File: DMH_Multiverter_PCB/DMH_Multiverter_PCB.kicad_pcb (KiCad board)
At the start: 2 copper layers, 48 x 175 mm, 0 parts

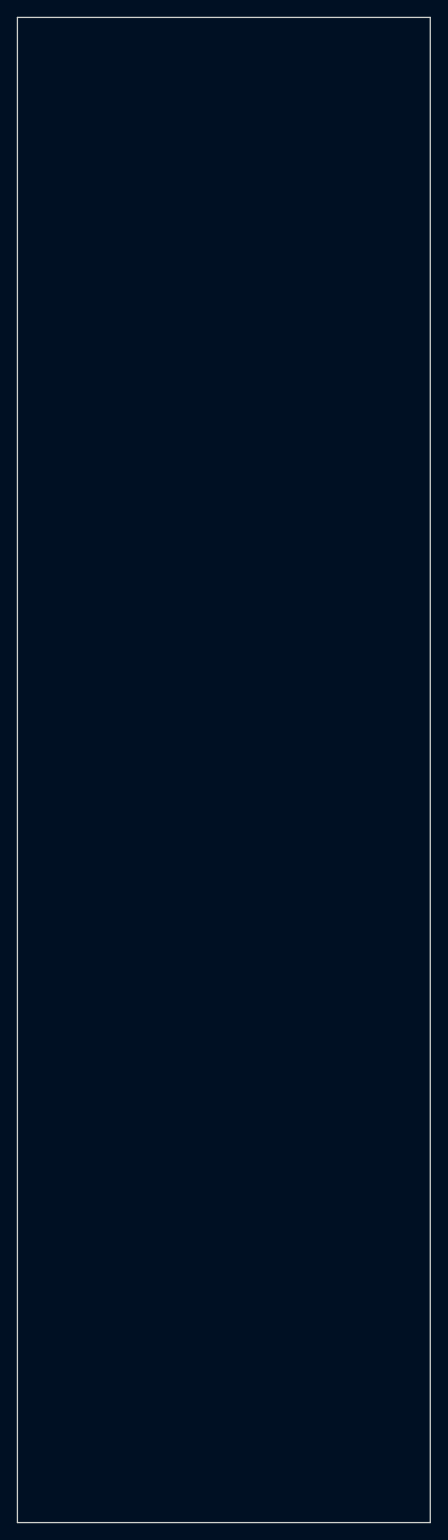
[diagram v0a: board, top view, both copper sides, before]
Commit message: Placed components in PCB
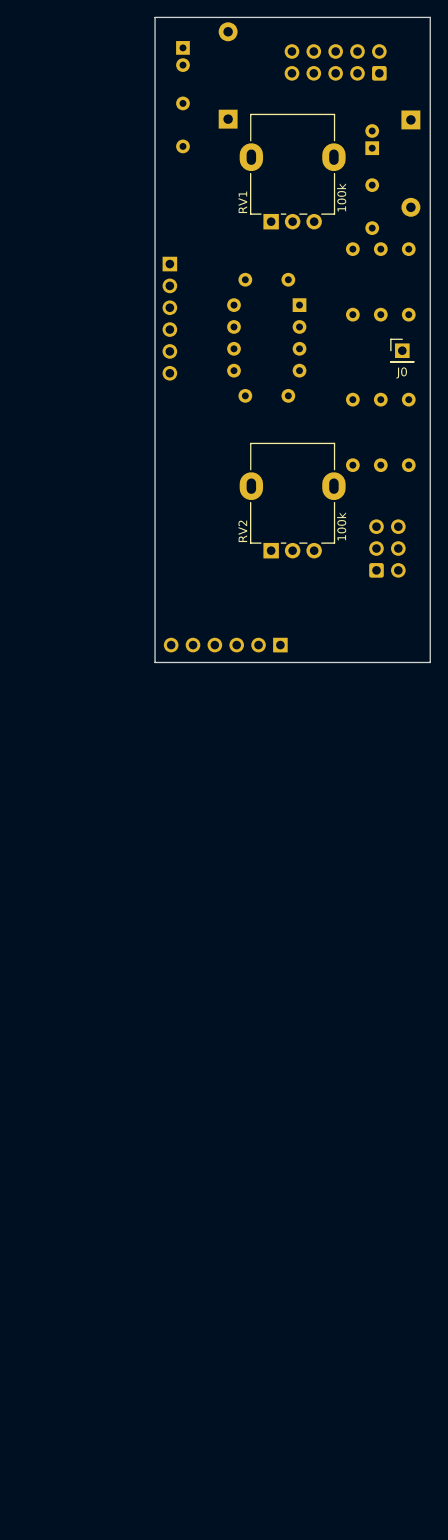
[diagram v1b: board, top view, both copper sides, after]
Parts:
- added C1: 47uF, Capacitor_THT:CP_Radial_D5.0mm_P2.00mm, B.Cu at (70.2, 46.0)
- added C2: 47uF, Capacitor_THT:CP_Radial_D5.0mm_P2.00mm, B.Cu at (92.2, 57.7)
- added C3: 100nF, Capacitor_THT:C_Disc_D4.3mm_W1.9mm_P5.00mm, B.Cu at (70.2, 57.5)
- added C4: 100nF, Capacitor_THT:C_Disc_D4.3mm_W1.9mm_P5.00mm, B.Cu at (92.2, 62.0)
- added C5: 100nF, Capacitor_THT:C_Disc_D4.3mm_W1.9mm_P5.00mm, B.Cu at (77.5, 73.0)
- added C6: 100nF, Capacitor_THT:C_Disc_D4.3mm_W1.9mm_P5.00mm, B.Cu at (82.5, 86.5)
- added D1: SB140+, Diode_THT:D_DO-41_SOD81_P10.16mm_Horizontal, B.Cu at (75.5, 54.3)
- added D2: SB140-, Diode_THT:D_DO-41_SOD81_P10.16mm_Horizontal, B.Cu at (96.8, 54.4)
- added J0: Conn_01x01, Connector_PinHeader_2.54mm:PinHeader_1x01_P2.54mm_Vertical, F.Cu at (95.8, 81.2)
- added J100: IDC_02x05, SynthStuff:IDC-Header_2x05_P2.54mm_Vertical_Eurorack, B.Cu at (93.1, 49.0)
- added J200: BackBone_Connector_6pin, SynthStuff:IDC-Header_2x03_P2.54mm_Vertical_BackBone, B.Cu at (92.7, 106.8)
- added J50: Conn_01x06, Connector_PinSocket_2.54mm:PinSocket_1x06_P2.54mm_Vertical, B.Cu at (68.7, 71.2)
- added J60: Conn_01x06, Connector_PinSocket_2.54mm:PinSocket_1x06_P2.54mm_Vertical, B.Cu at (81.6, 115.5)
- added R1: 100k, Resistor_THT:R_Axial_DIN0207_L6.3mm_D2.5mm_P7.62mm_Horizontal, B.Cu at (90.0, 69.4)
- added R2: 100k, Resistor_THT:R_Axial_DIN0207_L6.3mm_D2.5mm_P7.62mm_Horizontal, B.Cu at (93.2, 77.1)
- added R3: 1k, Resistor_THT:R_Axial_DIN0207_L6.3mm_D2.5mm_P7.62mm_Horizontal, B.Cu at (96.5, 69.4)
- added R4: 100k, Resistor_THT:R_Axial_DIN0207_L6.3mm_D2.5mm_P7.62mm_Horizontal, B.Cu at (90.0, 94.6)
- added R5: 100k, Resistor_THT:R_Axial_DIN0207_L6.3mm_D2.5mm_P7.62mm_Horizontal, B.Cu at (93.2, 94.6)
- added R6: 1k, Resistor_THT:R_Axial_DIN0207_L6.3mm_D2.5mm_P7.62mm_Horizontal, B.Cu at (96.5, 86.9)
- added RV1: 100k, SynthStuff:Potentiometer_Alpha_RD901F-40-00D_Single_Vertical, F.Cu at (80.5, 66.2)
- added RV2: 100k, SynthStuff:Potentiometer_Alpha_RD901F-40-00D_Single_Vertical, F.Cu at (80.5, 104.5)
- added U1: TL072, Package_DIP:DIP-8_W7.62mm_Socket, B.Cu at (83.8, 76.0)
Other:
- board size 48 x 175 mm -> 32 x 75 mm

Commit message: Finished PCB Conn schematic
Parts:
- moved C6 5.00 mm to (77.5, 86.5), turned to 0 degrees
- moved J50 0.25 mm to (69.0, 71.2)
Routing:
- net -12V: track 0.00 -> 46.5 mm
- net /Core Circuit/Att B Input: track 0.00 -> 40.4 mm
- net +12V: track 0.00 -> 40.1 mm
- net /Core Circuit/Att B Output: track 0.00 -> 35.7 mm
- net /Core Circuit/Att A Output: track 0.00 -> 30.0 mm
- net Net-(J200-Pin_4): track 0.00 -> 26.0 mm
- net Net-(U1B--): track 0.00 -> 25.2 mm
- net /Core Circuit/Att A Input: track 0.00 -> 24.4 mm
- net Net-(R5-Pad2): track 0.00 -> 23.8 mm
- net Net-(U1B-+): track 0.00 -> 23.8 mm
- net Net-(J200-Pin_3): track 0.00 -> 22.0 mm
- net Net-(J200-Pin_2): track 0.00 -> 18.4 mm
- net Net-(U1A-+): track 0.00 -> 16.5 mm
- net Net-(R2-Pad2): track 0.00 -> 15.4 mm
- net Net-(J200-Pin_1): track 0.00 -> 14.8 mm
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- added copper zone on B.Cu, net GND
- added copper zone on F.Cu, net GND

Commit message: Finished conn PCB
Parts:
- moved C1 9.09 mm to (75.0, 53.8)
- moved J60 7.75 mm to (89.3, 115.5)
- moved D1 5.80 mm to (69.8, 55.1)
- moved C3 2.30 mm to (69.8, 59.8), turned to -90 degrees
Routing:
- net +12V: track 40.1 -> 30.4 mm
- net Net-(D1-A): track 10.9 -> 16.3 mm
- net Net-(J200-Pin_4): track 26.0 -> 21.3 mm
- net Net-(J200-Pin_2): track 18.4 -> 13.7 mm
- net Net-(J200-Pin_1): track 14.8 -> 10.1 mm
- net Net-(J200-Pin_3): track 22.0 -> 17.3 mm

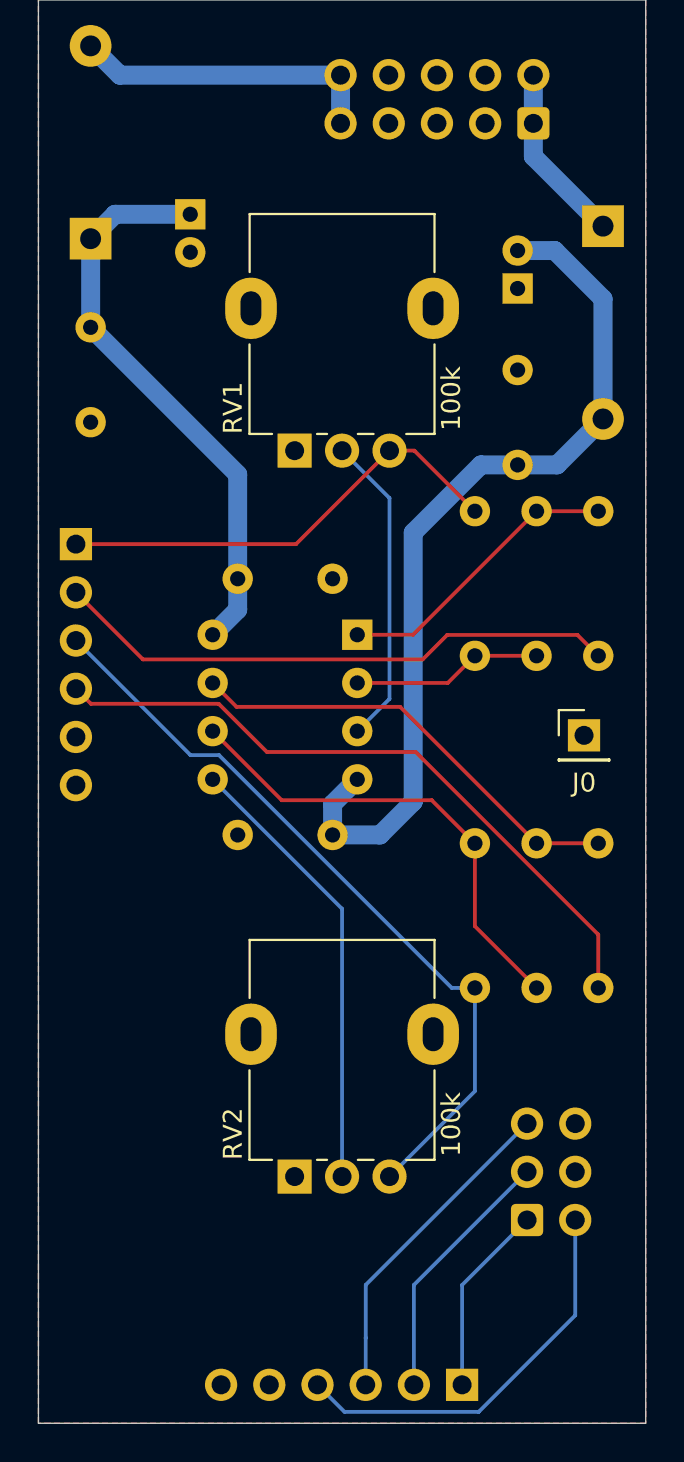
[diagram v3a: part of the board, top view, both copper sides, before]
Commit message: Adapted design to center detent pot P110KH-1F15
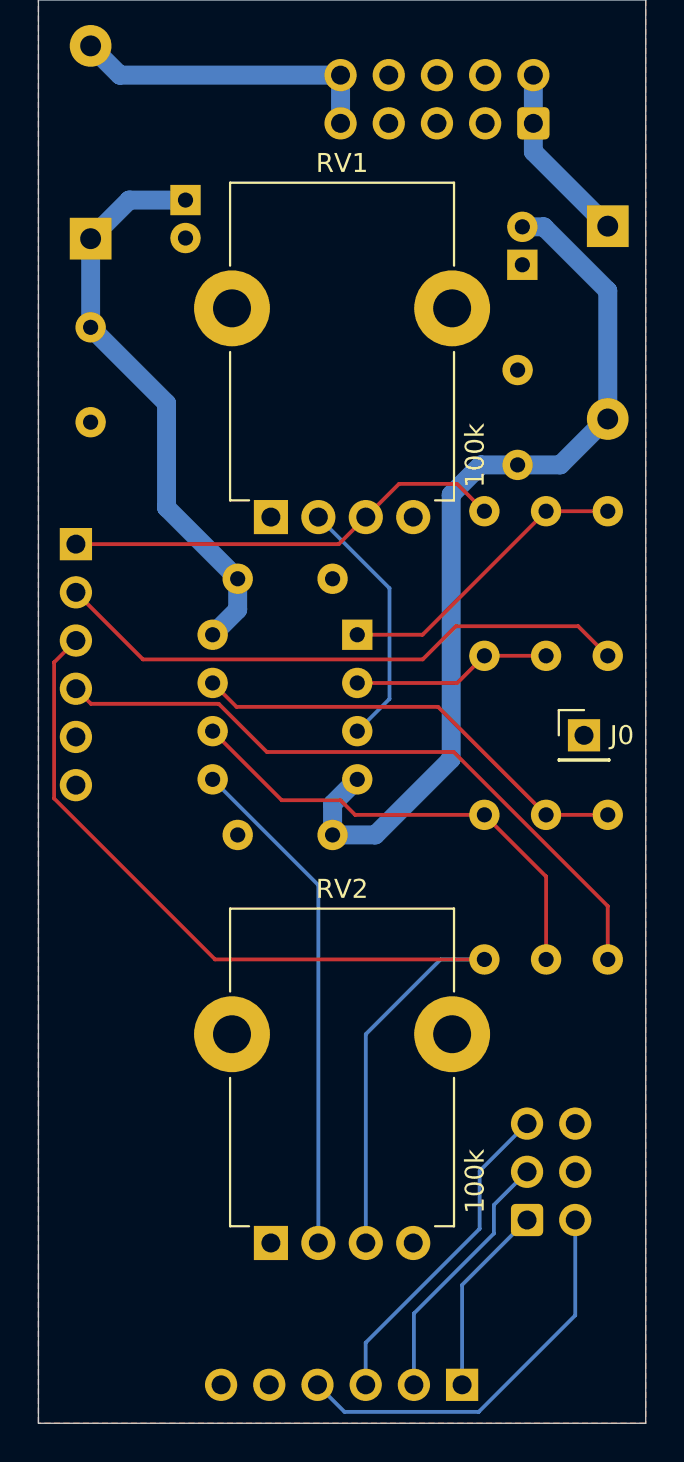
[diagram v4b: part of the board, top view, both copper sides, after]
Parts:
- RV1, RV2: footprint SynthStuff:Potentiometer_Alpha_RD901F-40-00D_Single_Vertical -> SynthStuff:Potentiometer_TT_P110KH1
- moved RV1 3.50 mm to (80.5, 69.8), turned to 0 degrees
- moved RV2 3.50 mm to (80.5, 108.0), turned to 0 degrees
- moved R4 1.58 mm to (90.5, 93.1)
- moved R5 1.58 mm to (93.8, 93.1)
- moved R6 1.58 mm to (97.0, 85.4)
- moved C2 1.27 mm to (92.5, 56.5)
- moved C1 0.79 mm to (74.8, 53.0)
- moved R1 0.50 mm to (90.5, 69.4)
- moved R2 0.50 mm to (93.8, 77.1)
- moved R3 0.50 mm to (97.0, 69.4)
- moved D2 0.25 mm to (97.0, 54.4)
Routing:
- net /Core Circuit/Att B Input: track 40.4 -> 53.9 mm
- net Net-(U1B-+): track 23.8 -> 26.7 mm
- net Net-(U1A-+): track 16.5 -> 13.5 mm
- net /Core Circuit/Att A Input: track 24.4 -> 23.4 mm
- net /Core Circuit/Att A Output: track 30.0 -> 30.9 mm
- net -12V: track 47.0 -> 47.9 mm
- net Net-(U1A--): track 10.0 -> 10.5 mm
- net Net-(R2-Pad2): track 15.4 -> 15.9 mm
